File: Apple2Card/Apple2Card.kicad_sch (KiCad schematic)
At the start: 59 parts, among them J1 ICSP, J2 Conn_01x25, J3 Conn_01x25, J4 Conn_01x16, J5 SERCON, J6 WIZNET 5500, SW1 SW_Push, U1 ATmega328P-P, U2 74HCT32, U3 74HCT00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

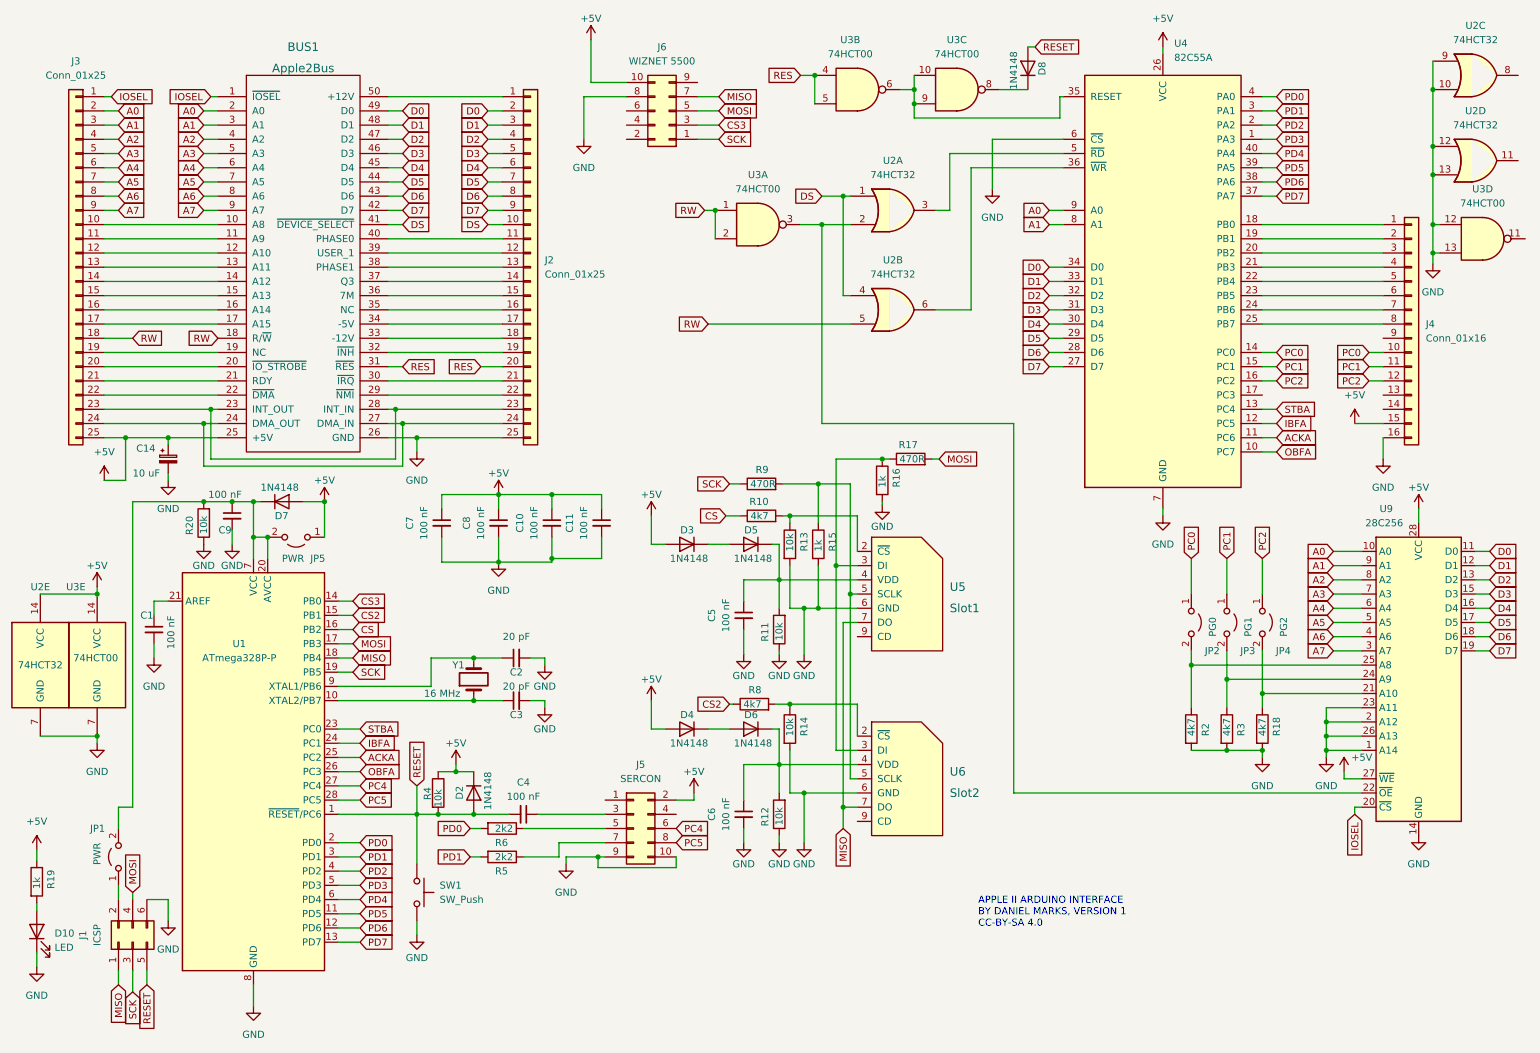
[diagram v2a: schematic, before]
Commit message: Added programming jumper
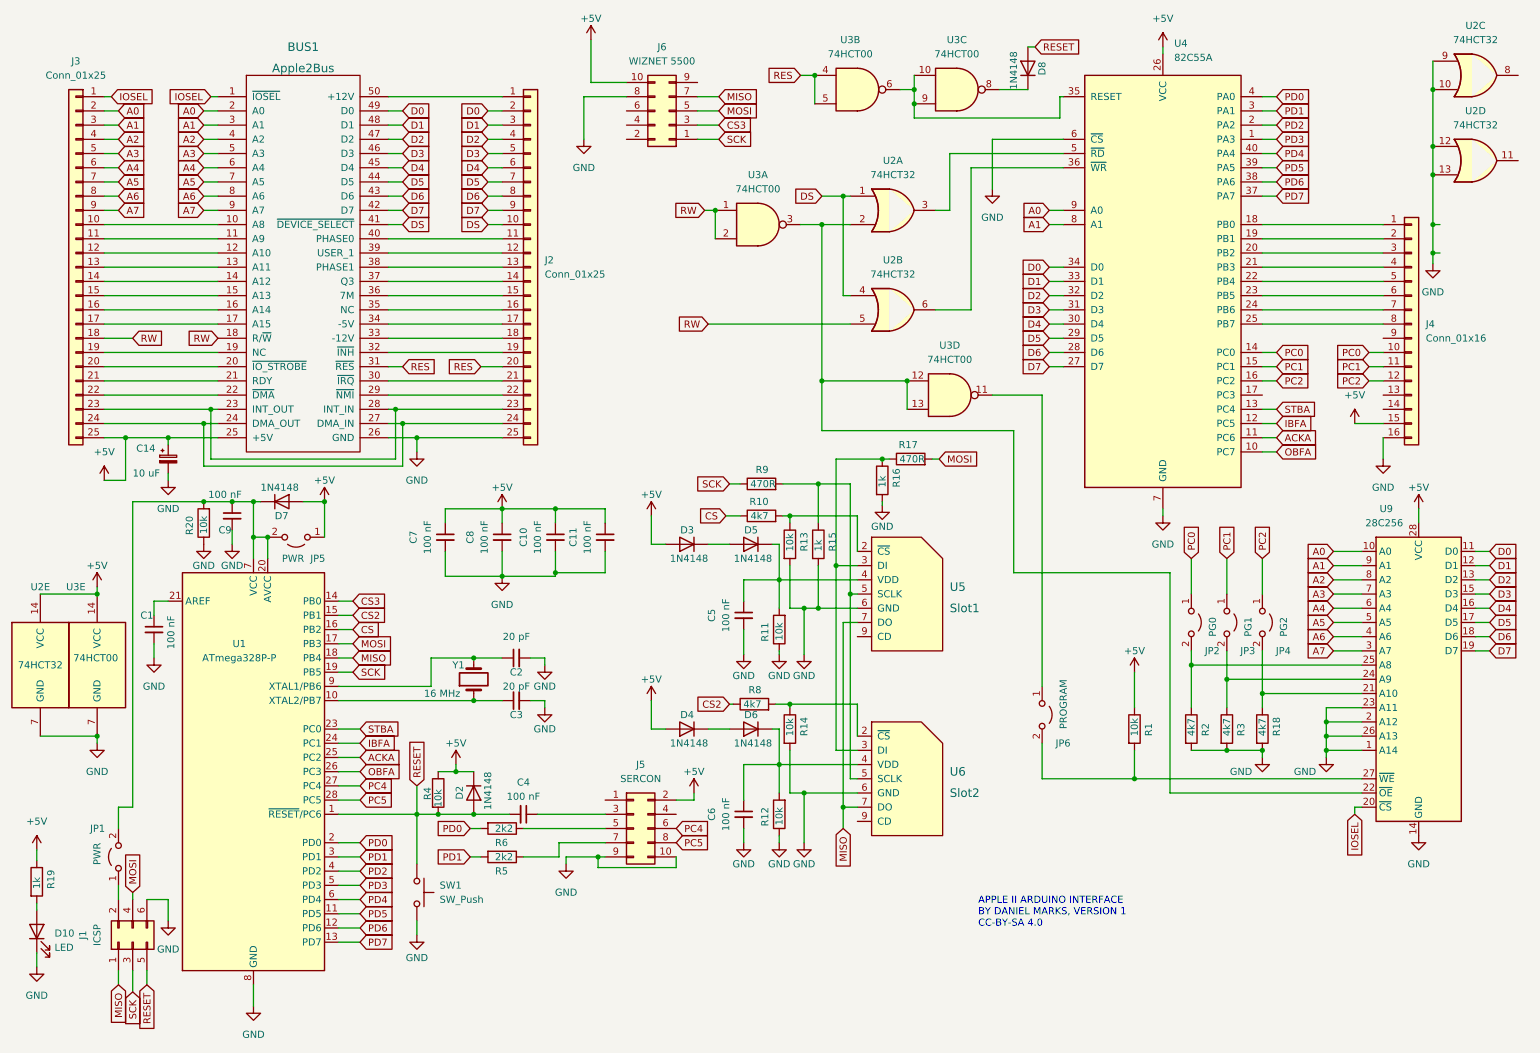
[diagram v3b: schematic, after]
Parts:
- added JP6: PROGRAM, Connector_PinHeader_2.54mm:PinHeader_1x02_P2.54mm_Vertical, symbol Jumper:Jumper_2_Open
- added R1: 10k, Resistor_THT:R_Axial_DIN0207_L6.3mm_D2.5mm_P7.62mm_Horizontal, symbol Device:R
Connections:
- net +5V: now also R1.1; no longer U9.27 (~{WE})
- net GND: no longer U3.12, U3.13
- net at U2.2, U3.3, U9.22 (~{OE}): now also U3.12, U3.13
- net at U3.11: now also JP6.1 (A)
- new net: JP6.2 (B), R1.2, U9.27 (~{WE})
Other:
- moved on the sheet: C10, C11, C7, C8, U3D

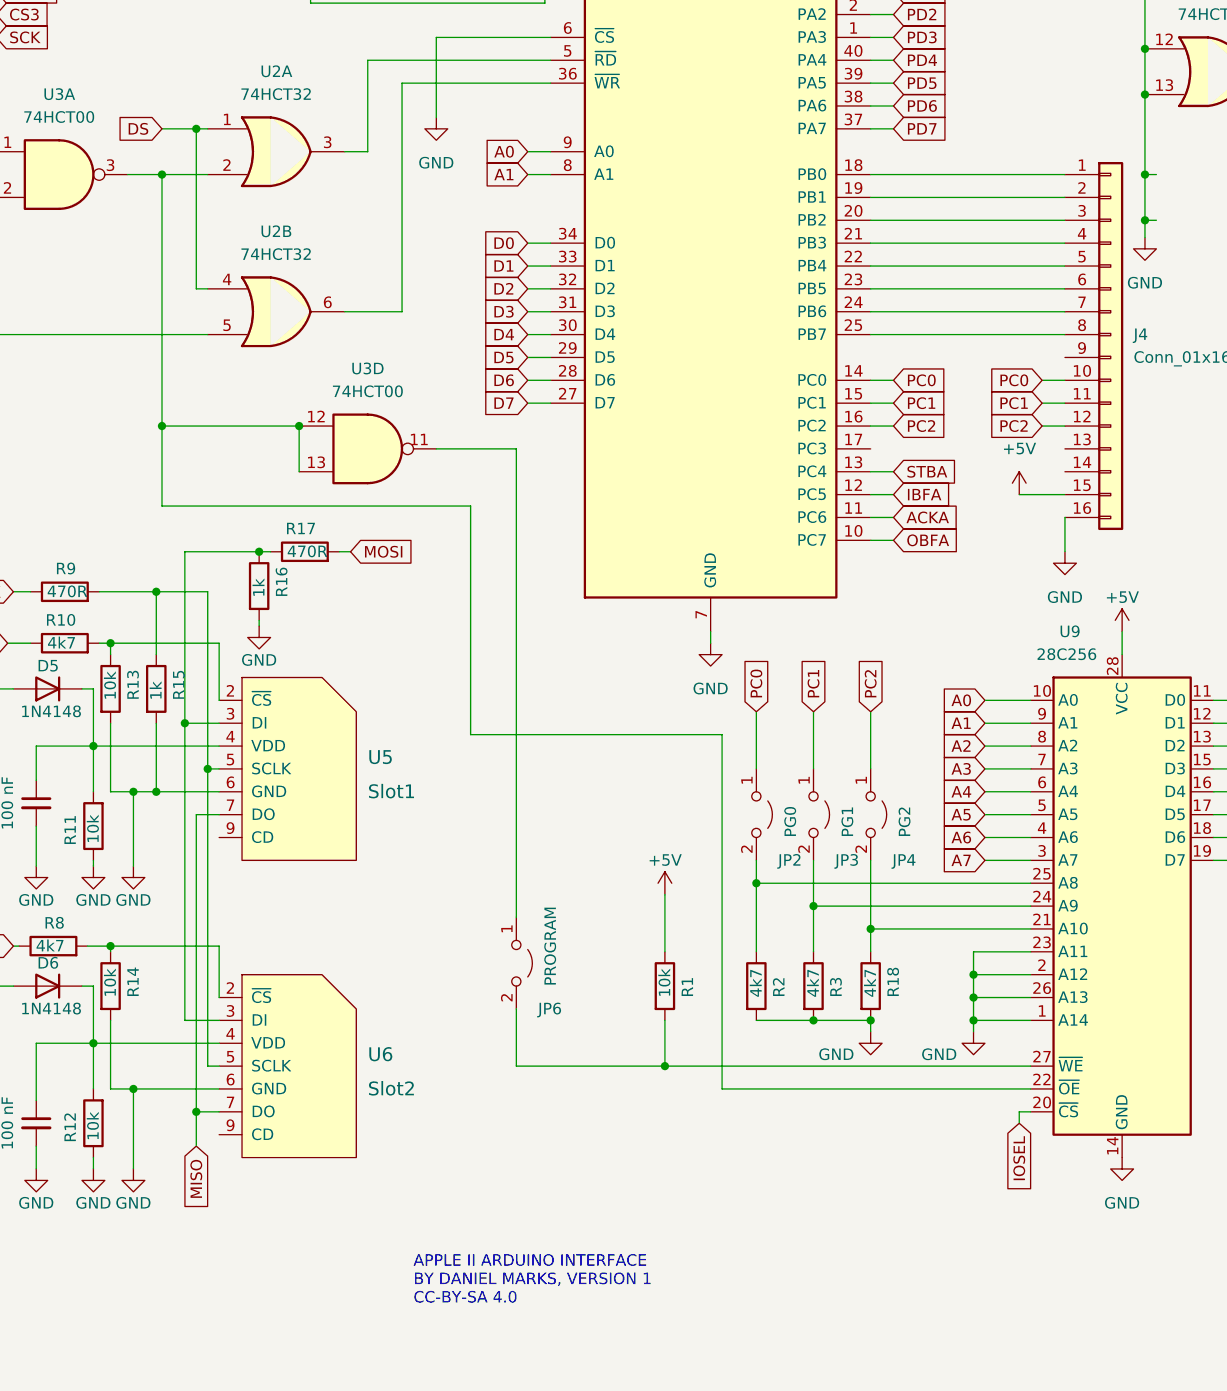
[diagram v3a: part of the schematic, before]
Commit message: Added other connections to 28C256 address lines
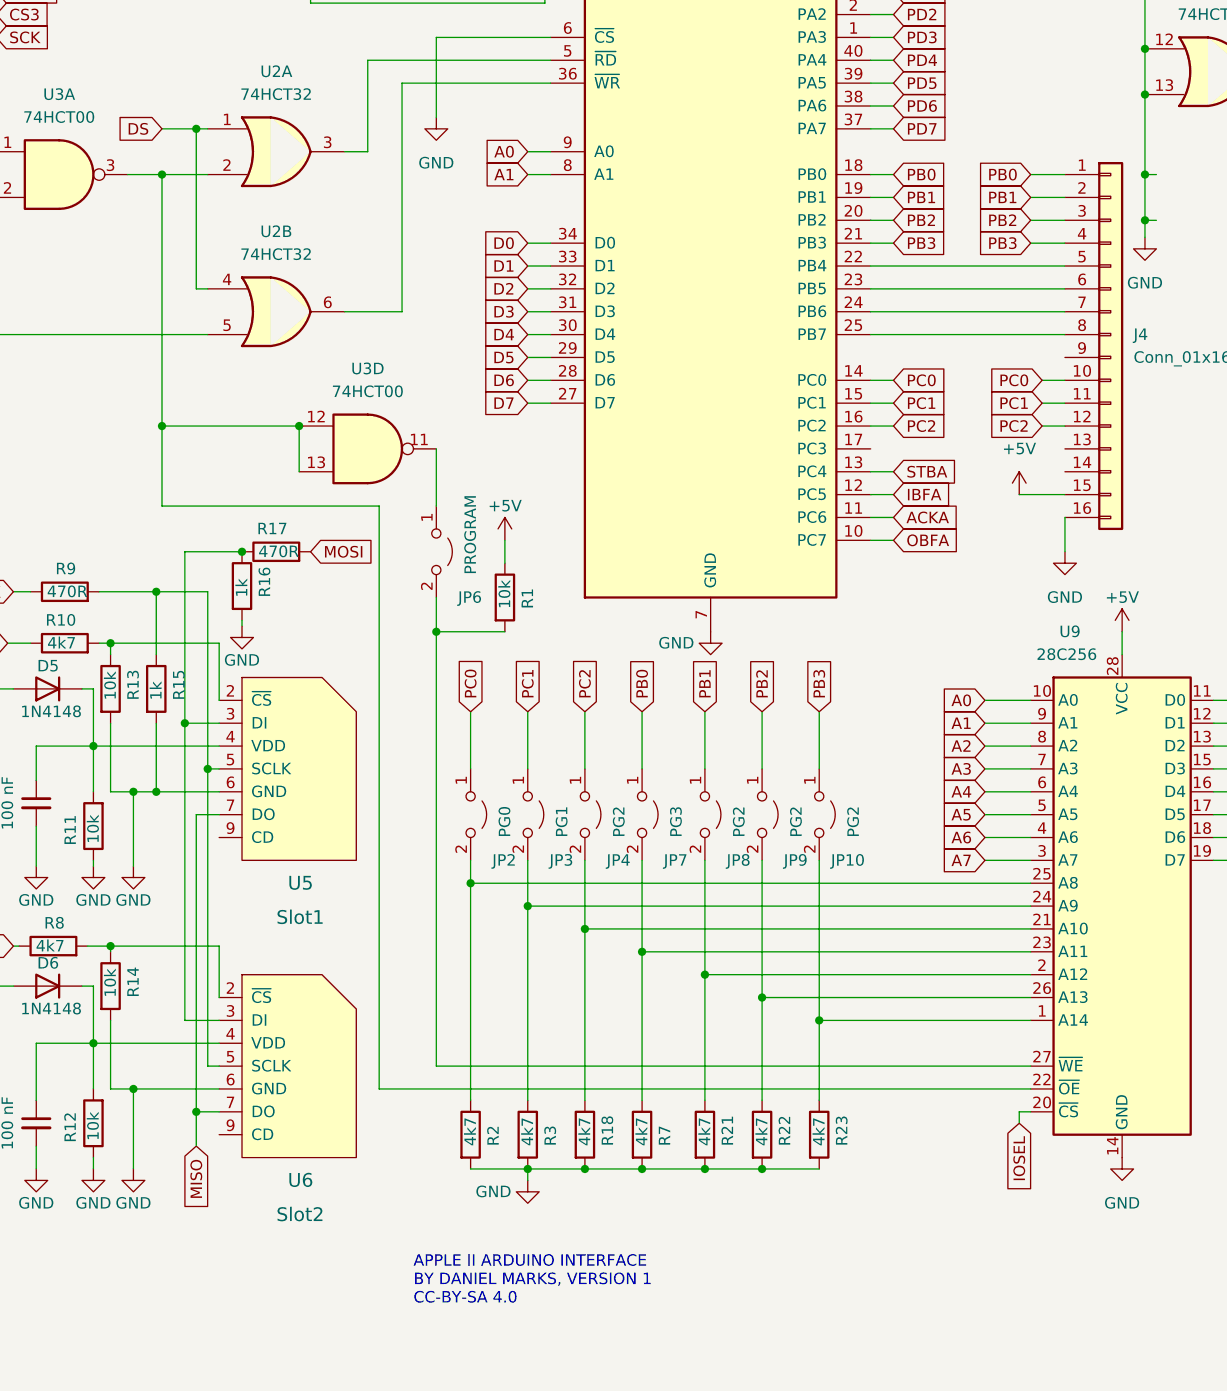
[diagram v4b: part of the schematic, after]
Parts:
- added JP10, JP8, JP9: PG2, Connector_PinHeader_2.54mm:PinHeader_1x02_P2.54mm_Vertical, symbol Jumper:Jumper_2_Open
- added JP7: PG3, Connector_PinHeader_2.54mm:PinHeader_1x02_P2.54mm_Vertical, symbol Jumper:Jumper_2_Open
- added R21, R22, R23, R7: 4k7, Resistor_THT:R_Axial_DIN0207_L6.3mm_D2.5mm_P7.62mm_Horizontal, symbol Device:R
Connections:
- net GND: now also R21.2, R22.2, R23.2, R7.2; no longer U9.1 (A14), U9.2 (A12), U9.23 (A11), U9.26 (A13)
- net PB0: now reaches J4.1 (Pin_1), U4.18 (PB0)
- net PB0: now also JP7.1 (A)
- net PB1: now reaches J4.2 (Pin_2), U4.19 (PB1)
- net PB1: now also JP8.1 (A)
- net PB2: now reaches J4.3 (Pin_3), U4.20 (PB2)
- net PB2: now also JP9.1 (A)
- net PB3: now reaches J4.4 (Pin_4), U4.21 (PB3)
- net PB3: now also JP10.1 (A)
- new net: JP9.2 (B), R22.1, U9.26 (A13)
- new net: JP10.2 (B), R23.1, U9.1 (A14)
- new net: JP8.2 (B), R21.1, U9.2 (A12)
- new net: JP7.2 (B), R7.1, U9.23 (A11)
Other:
- moved on the sheet: JP2, JP3, JP4, JP6, R1, R16, R17, R18, R2, R3

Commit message: JLCPCB order 2022-06-15
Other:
- moved on the sheet: U2B
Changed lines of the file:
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@@
   (junction (at 210.82 161.29) (diameter 0) (color 0 0 0 0)
   )
-  (junction (at 266.7 55.88) (diameter 0) (color 0 0 0 0)
-  )
   (junction (at 95.25 128.27) (diameter 0) (color 0 0 0 0)
   )
@@
   (junction (at 100.33 113.665) (diameter 0) (color 0 0 0 0)
   )
-  (junction (at 266.7 50.8) (diameter 0) (color 0 0 0 0)
-  )
   (junction (at 85.09 156.21) (diameter 0) (color 0 0 0 0)
   )
@@
     (stroke (width 0) (type default) (color 0 0 0 0))
   )
-  (wire (pts (xy 266.7 41.91) (xy 266.7 50.8))
-    (stroke (width 0) (type default) (color 0 0 0 0))
-  )
   (wire (pts (xy 149.86 147.32) (xy 149.86 152.4))
     (stroke (width 0) (type default) (color 0 0 0 0))
@@
     (stroke (width 0) (type default) (color 0 0 0 0))
   )
-  (wire (pts (xy 266.7 50.8) (xy 267.97 50.8))
-    (stroke (width 0) (type default) (color 0 0 0 0))
-  )
   (wire (pts (xy 94.615 158.75) (xy 96.52 158.75))
     (stroke (width 0) (type default) (color 0 0 0 0))
@@
     (stroke (width 0) (type default) (color 0 0 0 0))
   )
-  (wire (pts (xy 161.29 63.5) (xy 162.56 63.5))
-    (stroke (width 0) (type default) (color 0 0 0 0))
-  )
   (wire (pts (xy 117.475 165.735) (xy 117.475 163.83))
     (stroke (width 0) (type default) (color 0 0 0 0))
@@
     (stroke (width 0) (type default) (color 0 0 0 0))
   )
-  (wire (pts (xy 137.16 68.58) (xy 162.56 68.58))
+  (wire (pts (xy 137.16 68.58) (xy 161.29 68.58))
     (stroke (width 0) (type default) (color 0 0 0 0))
   )
@@
     (stroke (width 0) (type default) (color 0 0 0 0))
   )
-  (wire (pts (xy 266.7 55.88) (xy 266.7 57.785))
+  (wire (pts (xy 266.7 41.91) (xy 266.7 45.085))
     (stroke (width 0) (type default) (color 0 0 0 0))
   )
@@
     (stroke (width 0) (type default) (color 0 0 0 0))
   )
-  (wire (pts (xy 266.7 55.88) (xy 267.97 55.88))
-    (stroke (width 0) (type default) (color 0 0 0 0))
-  )
   (wire (pts (xy 236.22 68.58) (xy 257.81 68.58))
     (stroke (width 0) (type default) (color 0 0 0 0))
@@
     (stroke (width 0) (type default) (color 0 0 0 0))
   )
-  (wire (pts (xy 177.8 66.04) (xy 184.15 66.04))
+  (wire (pts (xy 176.53 66.04) (xy 184.15 66.04))
     (stroke (width 0) (type default) (color 0 0 0 0))
   )
@@
     (stroke (width 0) (type default) (color 0 0 0 0))
   )
-  (wire (pts (xy 266.7 55.88) (xy 266.7 50.8))
-    (stroke (width 0) (type default) (color 0 0 0 0))
-  )
   (wire (pts (xy 31.75 154.94) (xy 34.29 154.94))
     (stroke (width 0) (type default) (color 0 0 0 0))
@@
     (pin "1")
   )
-  (symbol (lib_id "74xx:74LS32") (at 170.18 66.04 0) (unit 2)
+  (symbol (lib_id "74xx:74LS32") (at 168.91 66.04 0) (unit 2)
     (in_bom yes) (on_board yes) (fields_autoplaced)
-    (property "Reference" "U2" (id 0) (at 170.18 57.15 0))
-    (property "Value" "74HCT32" (id 1) (at 170.18 59.69 0))
-    (property "Footprint" "Package_DIP:DIP-14_W7.62mm_Socket" (id 2) (at 170.18 66.04 0)
+    (property "Reference" "U2" (id 0) (at 168.91 57.15 0))
+    (property "Value" "74HCT32" (id 1) (at 168.91 59.69 0))
+    (property "Footprint" "Package_DIP:DIP-14_W7.62mm_Socket" (id 2) (at 168.91 66.04 0)
       (effects (font (size 1.27 1.27)) hide)
     )
-    (property "Datasheet" "http://www.ti.com/lit/gpn/sn74LS32" (id 3) (at 170.18 66.04 0)
+    (property "Datasheet" "http://www.ti.com/lit/gpn/sn74LS32" (id 3) (at 168.91 66.04 0)
       (effects (font (size 1.27 1.27)) hide)
     )
@@
     (pin "1")
   )
-  (symbol (lib_id "power:GND") (at 266.7 57.785 0) (unit 1)
+  (symbol (lib_id "power:GND") (at 266.7 45.085 0) (unit 1)
     (in_bom yes) (on_board yes) (fields_autoplaced)
-    (property "Reference" "#PWR0107" (id 0) (at 266.7 64.135 0)
+    (property "Reference" "#PWR0107" (id 0) (at 266.7 51.435 0)
       (effects (font (size 1.27 1.27)) hide)
     )
-    (property "Value" "GND" (id 1) (at 266.7 62.865 0))
-    (property "Footprint" "" (id 2) (at 266.7 57.785 0)
+    (property "Value" "GND" (id 1) (at 266.7 50.165 0))
+    (property "Footprint" "" (id 2) (at 266.7 45.085 0)
       (effects (font (size 1.27 1.27)) hide)
     )
-    (property "Datasheet" "" (id 3) (at 266.7 57.785 0)
+    (property "Datasheet" "" (id 3) (at 266.7 45.085 0)
       (effects (font (size 1.27 1.27)) hide)
     )
